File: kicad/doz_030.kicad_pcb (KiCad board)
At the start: 2 copper layers, 78.3 x 50 mm, 31 parts, among them J2 SWD, J3 LCD, J4 RGB, J5 DC-025, J6 Motor, Q1 IRLR2905, SW1 RotaryEncoder_Switch, SW3 MTS-101, U1 LM78M05_TO252, U2 XC6206PxxxMR, U3 STM32F030F4Px, U4 HX

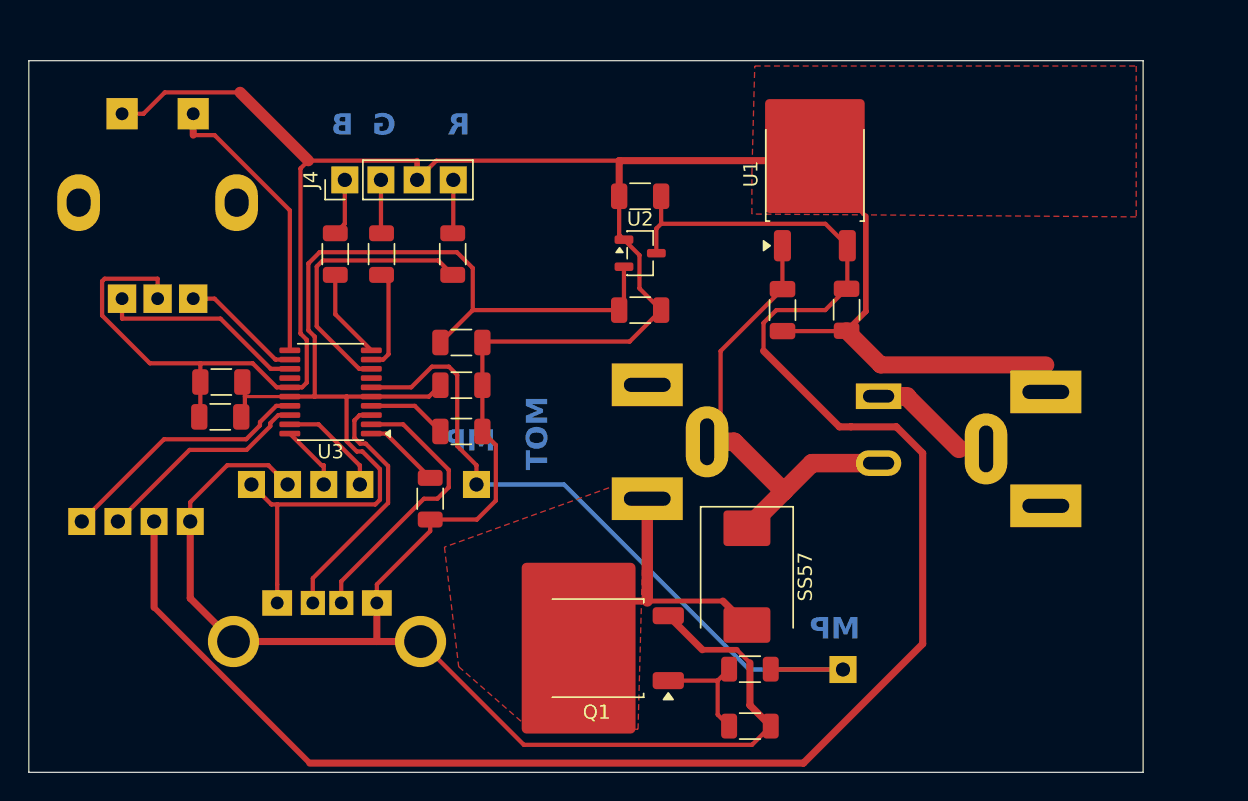
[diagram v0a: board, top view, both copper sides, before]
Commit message: Move current KiCad project into firmware repository
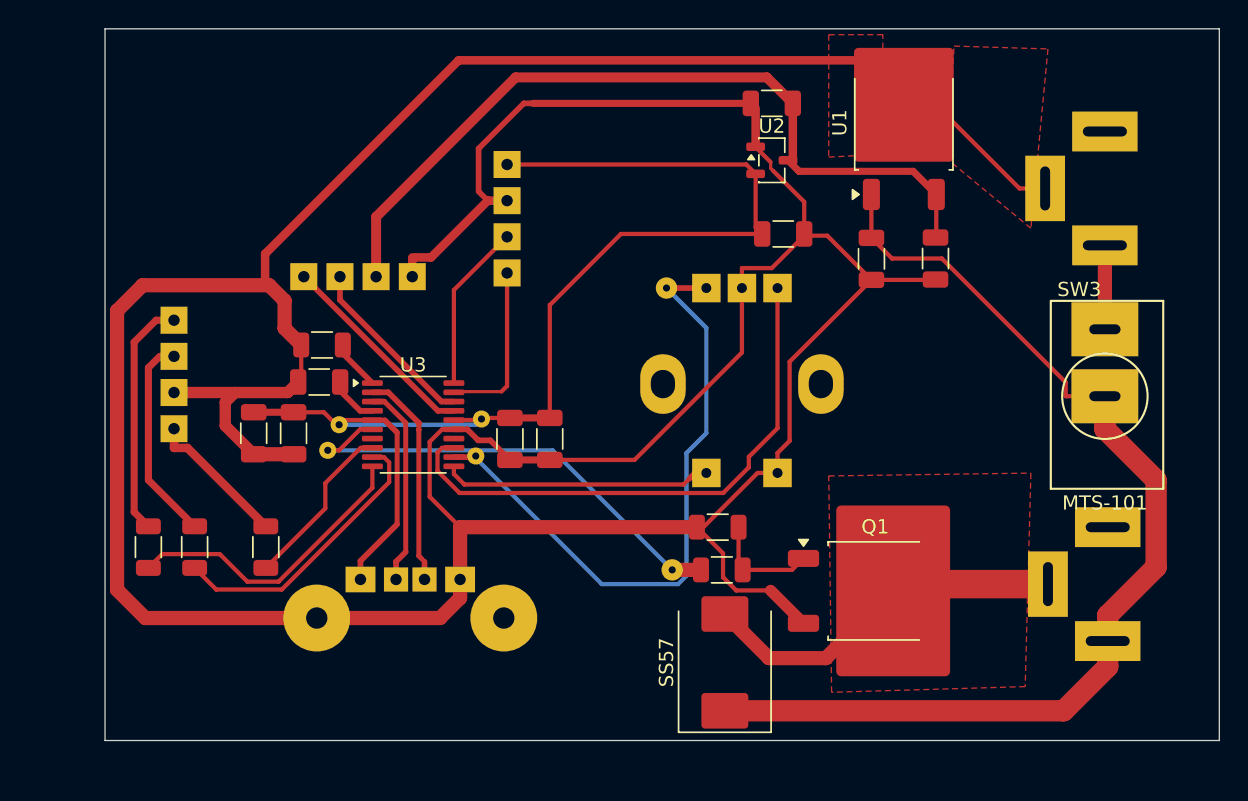
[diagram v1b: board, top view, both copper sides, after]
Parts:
- removed the ? at (85.2, 101.0)
- removed the ? at (111.0, 114.0)
- added ?: , , F.Cu at (85.2, 99.0)
- added ?: , , F.Cu at (74.8, 98.6)
- added ?: , , F.Cu at (98.6, 87.2)
- added ?: , , F.Cu at (99.0, 107.0)
- added TP1: +3.3V, Pin_1.2mm_Drill0.5mm, F.Cu at (75.6, 96.8)
- added TP2: +3.3V, Pin_1.2mm_Drill0.5mm, F.Cu at (85.6, 96.4)
- J4: moved to B.Cu
- SW3: moved to F.Cu
- moved SW1 43.1 mm to (103.9, 94.2), turned to 180 degrees
- moved J6 33.9 mm to (129.6, 108.0), turned to 180 degrees
- moved R2 24.4 mm to (70.5, 105.4)
- moved R3 24.4 mm to (65.5, 105.4)
- moved R4 24.4 mm to (62.2, 105.4)
- moved J3 23.2 mm to (73.1, 86.4)
- moved C7 23.2 mm to (90.4, 97.8), turned to -90 degrees
- moved C6 20.7 mm to (87.6, 97.8), turned to -90 degrees
- moved Q1 20.0 mm to (113.3, 108.5), turned to 0 degrees
- moved J5 18.8 mm to (129.4, 80.2)
- moved J2 18.1 mm to (87.4, 86.1), turned to 0 degrees
- moved SW3 16.6 mm to (129.4, 94.8), turned to 0 degrees
- moved C8 15.9 mm to (69.6, 97.4), turned to -90 degrees
- moved J4 15.5 mm to (64.0, 89.5), turned to 180 degrees
- moved R6 14.2 mm to (102.2, 104.0), turned to 0 degrees
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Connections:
- SW1 pad MP1: (no net) -> unconnected-(SW1-PadMP1)
- SW1 pad MP2: (no net) -> unconnected-(SW1-PadMP2)
- U4 pad 5: GND -> unconnected-(U4-GND-Pad5)
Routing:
- net +5V: track 125.3 -> 56.9 mm
- net GND: track 258.0 -> 305.9 mm
- net +12V: track 35.5 -> 74.7 mm
- net /CH1_R: track 8.56 -> 44.5 mm
- net /CH2_L: track 14.7 -> 39.3 mm
- net /Motor: track 51.4 -> 33.5 mm
- net /B: track 6.35 -> 21.2 mm
- net /G: track 7.14 -> 20.1 mm
- net Net-(J4-Pin_1): track 4.03 -> 16.8 mm
- net Net-(J4-Pin_2): track 3.77 -> 14.6 mm
- net /R: track 19.4 -> 12.0 mm
- net /SWCLK: track 4.66 -> 11.8 mm
- net Net-(J4-Pin_4): track 3.77 -> 10.1 mm
- net /M-: track 21.1 -> 26.1 mm
- net /DOUT: track 19.8 -> 15.3 mm
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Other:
- board text added: "MOTOR"
- board text removed: "MOT"
- board text removed: "MP"

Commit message: Update current KiCad board and keep latest LUT PDF
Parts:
- moved TP2 0.40 mm to (85.6, 96.0)
- moved TP1 0.40 mm to (75.6, 96.4)
- moved ? 0.20 mm to (85.2, 98.8)
